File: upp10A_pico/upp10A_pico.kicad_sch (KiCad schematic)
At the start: 71 parts, among them J1 Conn_01x20_Pin, J10 Conn_01x07, J11 Conn_01x03, J2 Conn_01x20_Pin, J3 Conn_01x03, J4 Conn_01x03, J5 Conn_01x05, J6 Conn_01x05, J7 Conn_01x05, J8 Conn_01x05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

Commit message: Correction in PCB project;
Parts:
- removed Q4, Q5, Q6, Q7: 2N7002, Package_TO_SOT_SMD:SOT-23, symbol Transistor_FET:2N7002
- added Q4, Q5, Q6, Q7: RK7002, Package_TO_SOT_SMD:SOT-23, symbol kpole:RK7002
- added unit 3 of U3
- C11: footprint (none) -> Capacitor_THT:CP_Radial_D6.3mm_P2.50mm
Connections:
- net +3.3V is gone; now on net +3V3: J2.5 (Pin_5), U4.16 (VCC)
- net +15V: now also U1.16 (Vdd), U3.14 (VDD)
- net GNDREF: now also U1.8 (Vss), Q4.1 (S), Q5.1 (S), Q6.1 (S), Q7.1 (S), U3.7 (VSS)
- net at J2.14 (Pin_14): now also Q4.2 (G)
- net at J2.15 (Pin_15): now also Q5.2 (G)
- net at J2.16 (Pin_16): now also Q6.2 (G)
- net at J2.17 (Pin_17): now also Q7.2 (G)
- net at J7.3 (Pin_3): now also Q6.3 (D)
- net at J7.4 (Pin_4): now also Q7.3 (D)
- net at R12.2: now also Q5.3 (D)
- net at R13.1: now also Q4.3 (D)
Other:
- moved on the sheet: U1B

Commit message: PCB: components layout;
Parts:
- removed J1, J2: Conn_01x20_Pin, Connector_PinHeader_2.54mm:PinHeader_1x20_P2.54mm_Vertical, symbol Connector:Conn_01x20_Pin
- added H1, H2, H3, H4: MountingHole, MountingHole:MountingHole_3.2mm_M3_Pad, symbol Mechanical:MountingHole
- added U7: RPi PICO, kpole:DIP-40_W700mils, symbol kpole:RP_Pico
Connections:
- net +3V3: now also U7.36
- net +5V: now also U7.40
- net GNDREF: now also U7.13, U7.18, U7.23, U7.28, U7.3, U7.33, U7.38, U7.8
- net at J10.3 (Pin_3), R9.2: now also U7.12
- net at D4.2 (A), D5.1 (K), R11.2: now also U7.31
- net at U4.10 (T2IN): now also U7.6
- net at U4.11 (T1IN): now also U7.1
- net at U4.12 (R1OUT): now also U7.2
- net at U4.9 (R2OUT): now also U7.7
- net at J10.4 (Pin_4), R27.2: now also U7.11
- net at J10.5 (Pin_5): now also U7.10
- net at J10.6 (Pin_6): now also U7.9
- net at Q4.2 (G): now also U7.27
- net at Q5.2 (G): now also U7.26
- net at Q6.2 (G): now also U7.25
- net at Q7.2 (G): now also U7.24
- net at Q1.2 (D): now also U7.22
- net at U2.3 (Y): now also U7.32
- net at J11.2 (Pin_2), R28.1: now also U7.20
- net at Q2.2 (D): now also U7.15
- net at Q3.2 (D): now also U7.16
- net at J11.1 (Pin_1), R29.1: now also U7.19
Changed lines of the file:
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@@
     (stroke (width 0) (type default))
   )
-  (wire (pts (xy 171.45 43.18) (xy 175.26 43.18))
-    (stroke (width 0) (type default))
-  )
   (wire (pts (xy 105.41 69.85) (xy 105.41 36.83))
     (stroke (width 0) (type default))
@@
     (stroke (width 0) (type default))
   )
+  (wire (pts (xy 171.45 43.18) (xy 175.26 43.18))
+    (stroke (width 0) (type default))
+  )
   (wire (pts (xy 105.41 36.83) (xy 113.03 36.83))
     (stroke (width 0) (type default))
@@
     (stroke (width 0) (type default))
   )
-  (text_box "RPi PICO"
-    (at 115.57 48.26 0) (size 15.24 50.8)
-    (stroke (width 0.2) (type default))
-    (fill (type none))
-    (effects (font (size 2 2)) (justify left top))
-  )
   (text "Pomiar\n +24V" (at 25.4 137.16 0)
     (effects (font (size 2 2)) (justify left bottom))
@@
     )
   )
-  (symbol (lib_id "Connector:Conn_01x20_Pin") (at 130.81 72.39 0) (unit 1)
-    (in_bom yes) (on_board yes) (dnp no) (fields_autoplaced)
-    (property "Reference" "J2" (at 131.445 46.99 0)
-      (effects (font (size 1.27 1.27)))
-    )
-    (property "Value" "Conn_01x20_Pin" (at 131.445 46.99 0)
-      (effects (font (size 1.27 1.27)) hide)
-    )
-    (property "Footprint" "Connector_PinHeader_2.54mm:PinHeader_1x20_P2.54mm_Vertical" (at 130.81 72.39 0)
-      (effects (font (size 1.27 1.27)) hide)
-    )
-    (property "Datasheet" "~" (at 130.81 72.39 0)
-      (effects (font (size 1.27 1.27)) hide)
-    )
-    (pin "19")
-    (pin "17")
-    (pin "7")
-    (pin "9")
-    (pin "8")
-    (pin "20")
-    (pin "16")
-    (pin "2")
-    (pin "15")
-    (pin "3")
-    (pin "1")
-    (pin "10")
-    (pin "11")
-    (pin "12")
-    (pin "13")
-    (pin "14")
-    (pin "18")
-    (pin "5")
-    (pin "4")
-    (pin "6")
-    (instances
-      (project "upp10A_pico"
-        (path "/0ec2864b-91a1-4031-905c-a0d4a4f4b48a"
-          (reference "J2") (unit 1)
-        )
-      )
-    )
-  )
   (symbol (lib_id "Device:C") (at 247.65 121.92 0) (unit 1)
     (in_bom yes) (on_board yes) (dnp no)
@@
     )
   )
+  (symbol (lib_id "Mechanical:MountingHole") (at 152.4 182.88 0) (unit 1)
+    (in_bom yes) (on_board yes) (dnp no) (fields_autoplaced)
+    (property "Reference" "H2" (at 154.94 182.88 0)
+      (effects (font (size 1.27 1.27)) (justify left))
+    )
+    (property "Value" "MountingHole" (at 154.94 184.15 0)
+      (effects (font (size 1.27 1.27)) (justify left) hide)
+    )
+    (property "Footprint" "MountingHole:MountingHole_3.2mm_M3_Pad" (at 152.4 182.88 0)
+      (effects (font (size 1.27 1.27)) hide)
+    )
+    (property "Datasheet" "~" (at 152.4 182.88 0)
+      (effects (font (size 1.27 1.27)) hide)
+    )
+    (instances
+      (project "upp10A_pico"
+        (path "/0ec2864b-91a1-4031-905c-a0d4a4f4b48a"
+          (reference "H2") (unit 1)
+        )
+      )
+    )
+  )
   (symbol (lib_id "power:GNDREF") (at 152.4 132.08 0) (unit 1)
     (in_bom yes) (on_board yes) (dnp no) (fields_autoplaced)
@@
     )
   )
-  (symbol (lib_id "Connector:Conn_01x20_Pin") (at 115.57 72.39 0) (mirror y) (unit 1)
-    (in_bom yes) (on_board yes) (dnp no)
-    (property "Reference" "J1" (at 115.57 46.99 0)
-      (effects (font (size 1.27 1.27)))
-    )
-    (property "Value" "Conn_01x20_Pin" (at 114.935 46.99 0)
-      (effects (font (size 1.27 1.27)) hide)
-    )
-    (property "Footprint" "Connector_PinHeader_2.54mm:PinHeader_1x20_P2.54mm_Vertical" (at 115.57 72.39 0)
-      (effects (font (size 1.27 1.27)) hide)
-    )
-    (property "Datasheet" "~" (at 115.57 72.39 0)
-      (effects (font (size 1.27 1.27)) hide)
-    )
-    (pin "19")
-    (pin "9")
-    (pin "6")
-    (pin "7")
-    (pin "8")
-    (pin "18")
-    (pin "3")
-    (pin "4")
-    (pin "2")
-    (pin "20")
-    (pin "5")
-    (pin "16")
-    (pin "15")
-    (pin "17")
-    (pin "1")
-    (pin "10")
-    (pin "11")
-    (pin "12")
-    (pin "13")
-    (pin "14")
-    (instances
-      (project "upp10A_pico"
-        (path "/0ec2864b-91a1-4031-905c-a0d4a4f4b48a"
-          (reference "J1") (unit 1)
-        )
-      )
-    )
-  )
   (symbol (lib_id "Device:R") (at 40.64 129.54 180) (unit 1)
     (in_bom yes) (on_board yes) (dnp no)
@@
     )
   )
+  (symbol (lib_id "Mechanical:MountingHole") (at 152.4 193.04 0) (unit 1)
+    (in_bom yes) (on_board yes) (dnp no) (fields_autoplaced)
+    (property "Reference" "H4" (at 154.94 193.04 0)
+      (effects (font (size 1.27 1.27)) (justify left))
+    )
+    (property "Value" "MountingHole" (at 154.94 194.31 0)
+      (effects (font (size 1.27 1.27)) (justify left) hide)
+    )
+    (property "Footprint" "MountingHole:MountingHole_3.2mm_M3_Pad" (at 152.4 193.04 0)
+      (effects (font (size 1.27 1.27)) hide)
+    )
+    (property "Datasheet" "~" (at 152.4 193.04 0)
+      (effects (font (size 1.27 1.27)) hide)
+    )
+    (instances
+      (project "upp10A_pico"
+        (path "/0ec2864b-91a1-4031-905c-a0d4a4f4b48a"
+          (reference "H4") (unit 1)
+        )
+      )
+    )
+  )
   (symbol (lib_id "Device:R") (at 175.26 46.99 0) (unit 1)
     (in_bom yes) (on_board yes) (dnp no)
@@
     )
   )
+  (symbol (lib_id "Mechanical:MountingHole") (at 152.4 187.96 0) (unit 1)
+    (in_bom yes) (on_board yes) (dnp no) (fields_autoplaced)
+    (property "Reference" "H3" (at 154.94 187.96 0)
+      (effects (font (size 1.27 1.27)) (justify left))
+    )
+    (property "Value" "MountingHole" (at 154.94 189.23 0)
+      (effects (font (size 1.27 1.27)) (justify left) hide)
+    )
+    (property "Footprint" "MountingHole:MountingHole_3.2mm_M3_Pad" (at 152.4 187.96 0)
+      (effects (font (size 1.27 1.27)) hide)
+    )
+    (property "Datasheet" "~" (at 152.4 187.96 0)
+      (effects (font (size 1.27 1.27)) hide)
+    )
+    (instances
+      (project "upp10A_pico"
+        (path "/0ec2864b-91a1-4031-905c-a0d4a4f4b48a"
+          (reference "H3") (unit 1)
+        )
+      )
+    )
+  )
   (symbol (lib_id "Device:R") (at 53.34 129.54 0) (unit 1)
     (in_bom yes) (on_board yes) (dnp no)
@@
     )
   )
+  (symbol (lib_id "Mechanical:MountingHole") (at 152.4 177.8 0) (unit 1)
+    (in_bom yes) (on_board yes) (dnp no) (fields_autoplaced)
+    (property "Reference" "H1" (at 154.94 176.53 0)
+      (effects (font (size 1.27 1.27)) (justify left))
+    )
+    (property "Value" "MountingHole" (at 154.94 179.07 0)
+      (effects (font (size 1.27 1.27)) (justify left))
+    )
+    (property "Footprint" "MountingHole:MountingHole_3.2mm_M3_Pad" (at 152.4 177.8 0)
+      (effects (font (size 1.27 1.27)) hide)
+    )
+    (property "Datasheet" "~" (at 152.4 177.8 0)
+      (effects (font (size 1.27 1.27)) hide)
+    )
+    (instances
+      (project "upp10A_pico"
+        (path "/0ec2864b-91a1-4031-905c-a0d4a4f4b48a"
+          (reference "H1") (unit 1)
+        )
+      )
+    )
+  )
   (symbol (lib_id "Device:R") (at 53.34 137.16 180) (unit 1)
     (in_bom yes) (on_board yes) (dnp no)
@@
         )
       )
+    )
+  )
+  (symbol (lib_id "kpole:RP_Pico") (at 110.49 49.53 0) (unit 1)
+    (in_bom yes) (on_board yes) (dnp no)
+    (property "Reference" "U7" (at 129.54 44.45 0)
+      (effects (font (size 1.27 1.27)))
+    )
+    (property "Value" "RPi PICO" (at 127 46.99 0)
+      (effects (font (size 1.27 1.27)))
+    )
+    (property "Footprint" "kpole:DIP-40_W700mils" (at 113.03 49.53 0)
+      (effects (font (size 1.27 1.27)) hide)
+    )
+    (property "Datasheet" "" (at 113.03 49.53 0)
+      (effects (font (size 1.27 1.27)) hide)
+    )
+    (pin "22")
+    (pin "7")
+    (pin "20")
+    (pin "27")
+    (pin "17")
+    (pin "18")
+    (pin "26")
+    (pin "38")
+    (pin "39")
+    (pin "19")
+    (pin "8")
+    (pin "4")
+    (pin "2")
+    (pin "40")
+    (pin "9")
+    (pin "10")
+    (pin "30")
+    (pin "28")
+    (pin "36")
+    (pin "29")
+    (pin "37")
+    (pin "25")
+    (pin "3")
+    (pin "32")
+    (pin "33")
+    (pin "34")
+    (pin "35")
+    (pin "13")
+    (pin "16")
+    (pin "1")
+    (pin "5")
+    (pin "21")
+    (pin "14")
+    (pin "23")
+    (pin "11")
+    (pin "15")
+    (pin "24")
+    (pin "12")
+    (pin "31")
+    (pin "6")
+    (instances
+      (project "upp10A_pico"
+        (path "/0ec2864b-91a1-4031-905c-a0d4a4f4b48a"
+          (reference "U7") (unit 1)
+        )
+      )

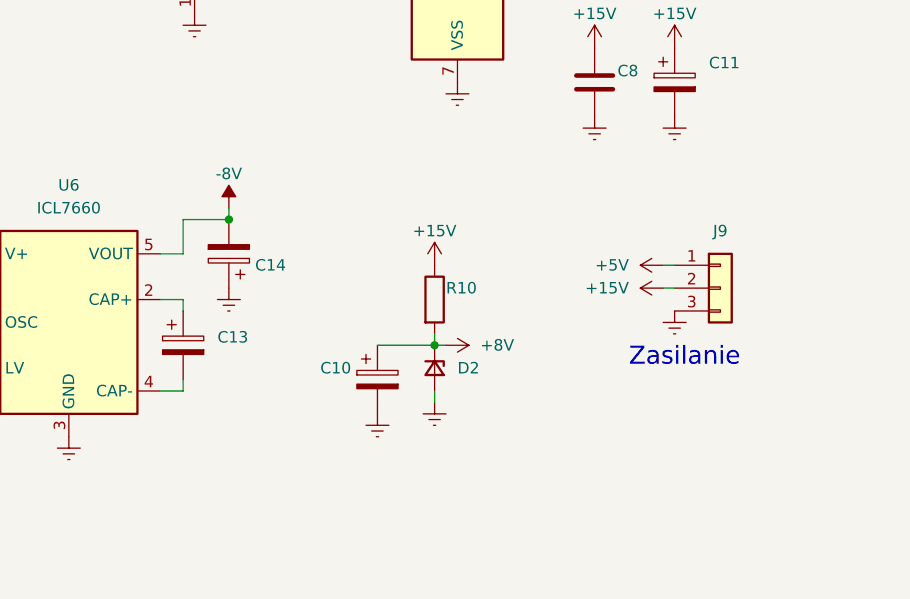
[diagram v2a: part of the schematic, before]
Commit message: PCB routing completed;
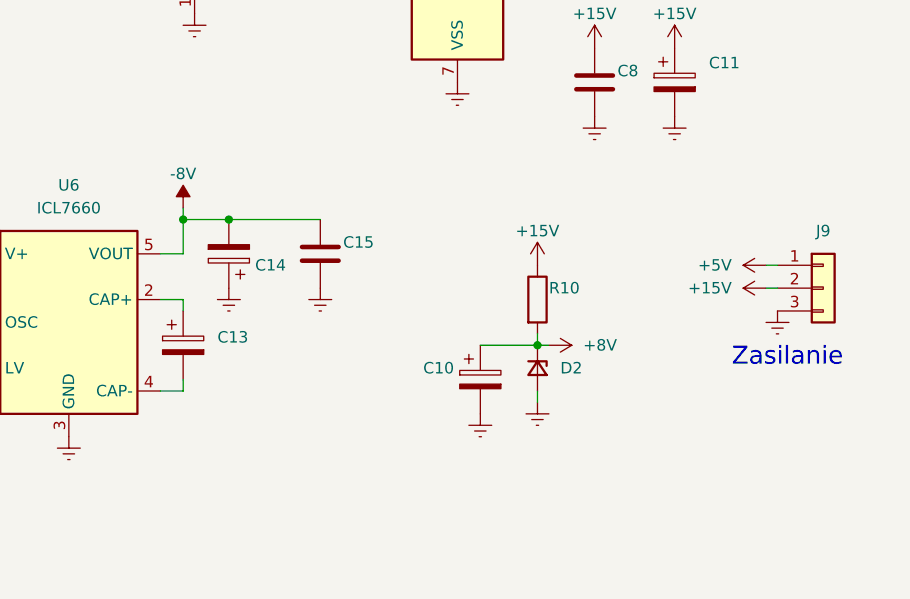
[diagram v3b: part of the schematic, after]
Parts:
- added C15: C, Capacitor_SMD:C_0805_2012Metric_Pad1.18x1.45mm_HandSolder, symbol Device:C
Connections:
- net -8V: now also C15.1
- net GNDREF: now also C15.2
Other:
- moved on the sheet: C10, D2, J9, R10

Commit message: Made corrections on PCB; added gerber files; added schematic in pdf;
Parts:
- added J1, J12, J2: Conn_01x01, Connector_Pin:Pin_D1.0mm_L10.0mm, symbol Connector_Generic:Conn_01x01
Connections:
- net at U7.21: now also J12.1 (Pin_1)
- net at U7.4: now also J1.1 (Pin_1)
- net at U7.5: now also J2.1 (Pin_1)
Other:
- moved on the sheet: C5, D4, D5, R11, R21, R22, R23, R24, R25, R26, U5, U7
